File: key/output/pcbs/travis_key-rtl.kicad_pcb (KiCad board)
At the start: 2 copper layers, 38.1 x 38.1 mm, 4 parts

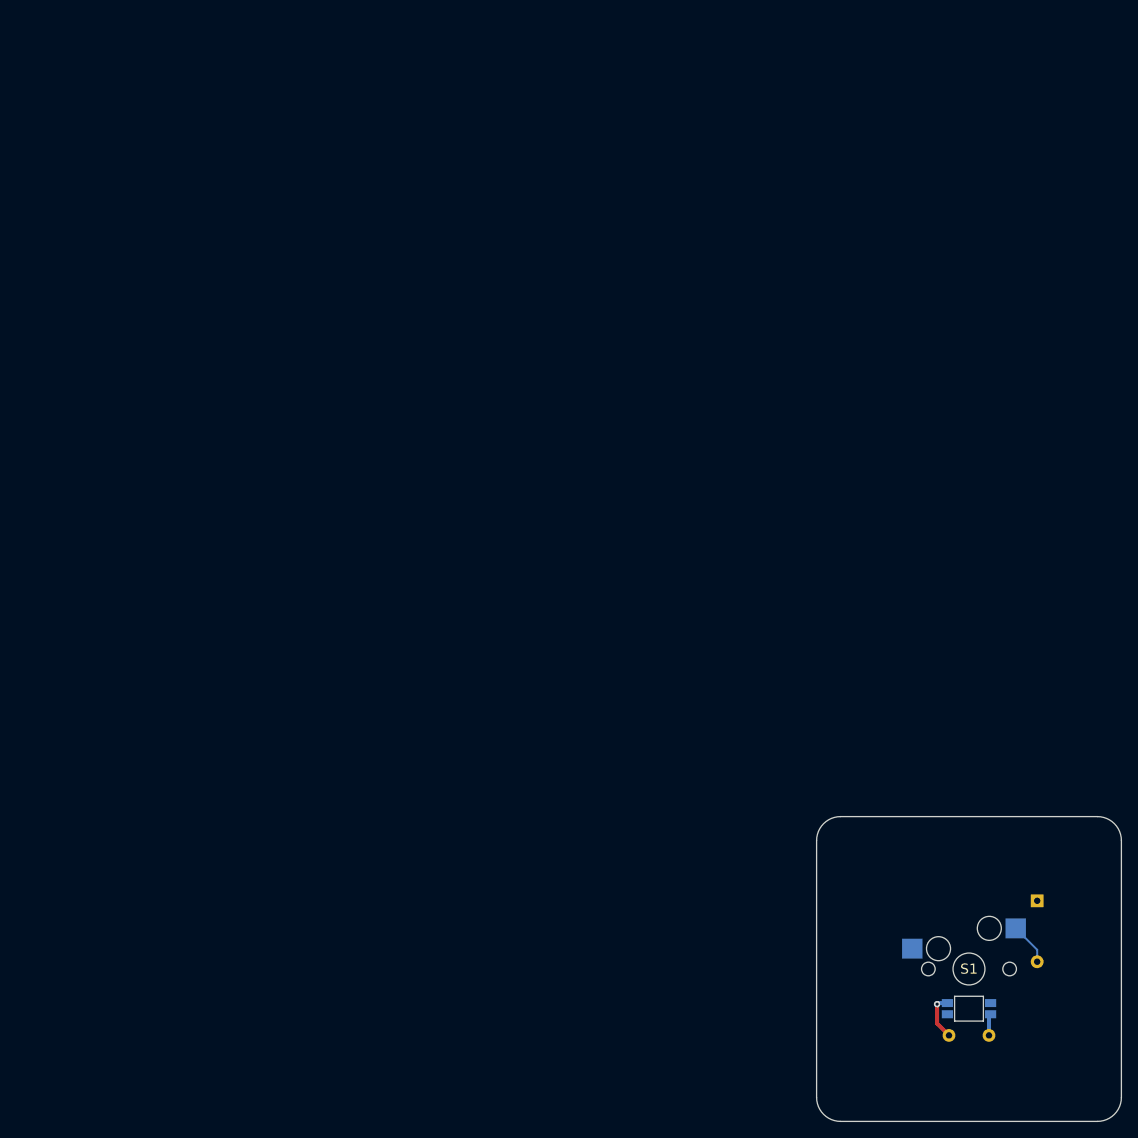
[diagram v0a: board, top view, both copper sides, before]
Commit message: key module functions with traces
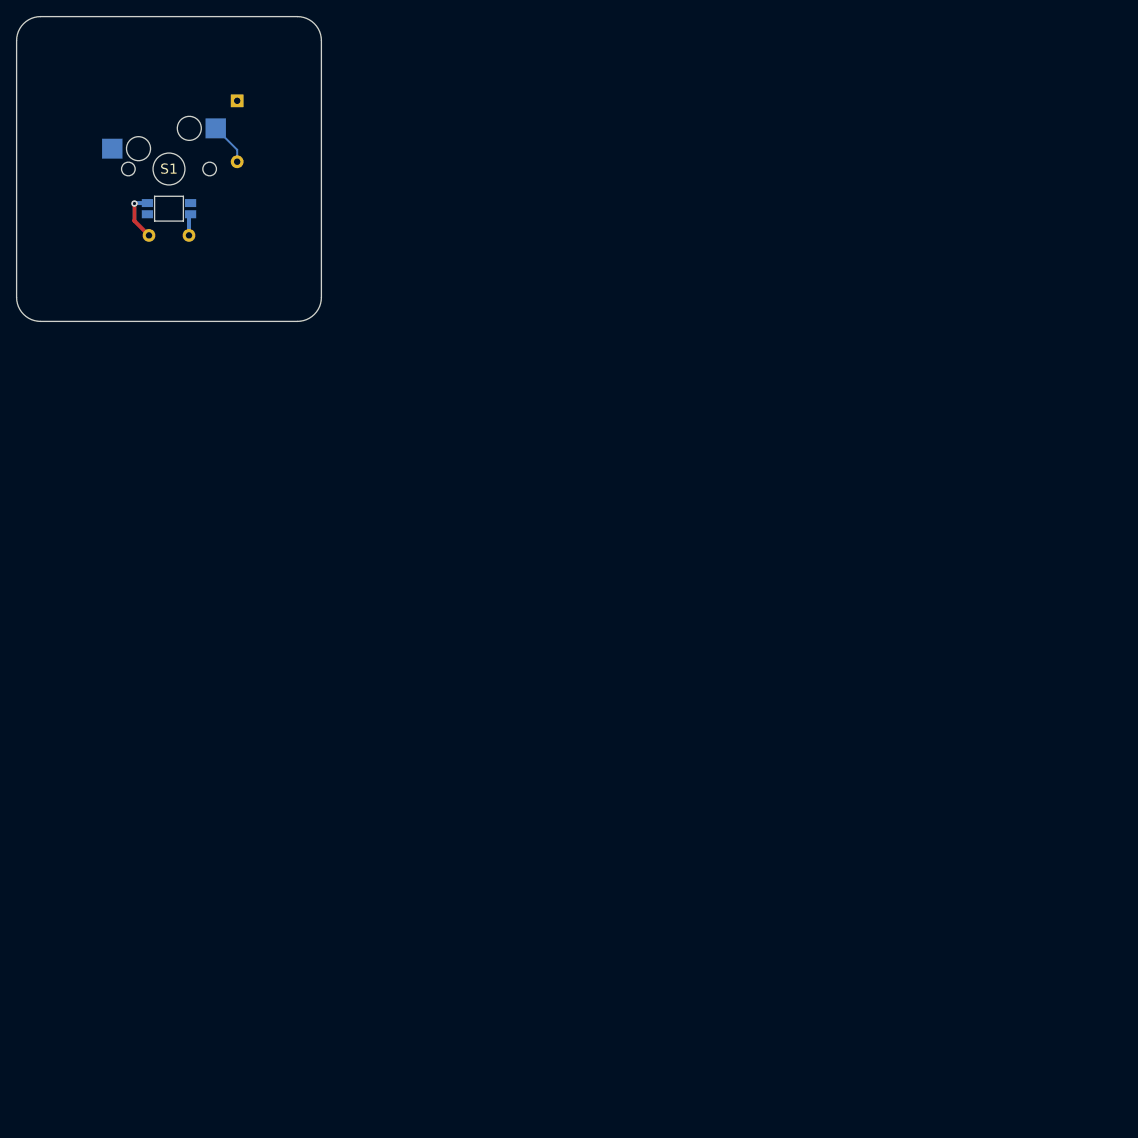
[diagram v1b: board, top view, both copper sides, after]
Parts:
- moved C1 141.4 mm to (2.50, 8.30)
- moved D1 141.4 mm to (8.53, -8.53)
- moved LED1 141.4 mm to (0.00, 4.96)
- moved S1 141.4 mm to (0.00, 0.00)
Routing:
- net GND: track 5.87 -> 6.38 mm
